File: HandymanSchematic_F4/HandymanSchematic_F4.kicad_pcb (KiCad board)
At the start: 4 copper layers, 55.6 x 45.5 mm, 79 parts, among them J1 SWD Header, J2 JACKS, J5 ScopeGroundLoop, Q1 BC847, Q2 2N7002, Q3 2N7002, SW1 RST, SW2 BYP, SW302 BOOT, U2 TL074, U3 STM32F411RETx, U4 AMS1117, U5 SSD1306, U6 TL072, Y1 16MHz

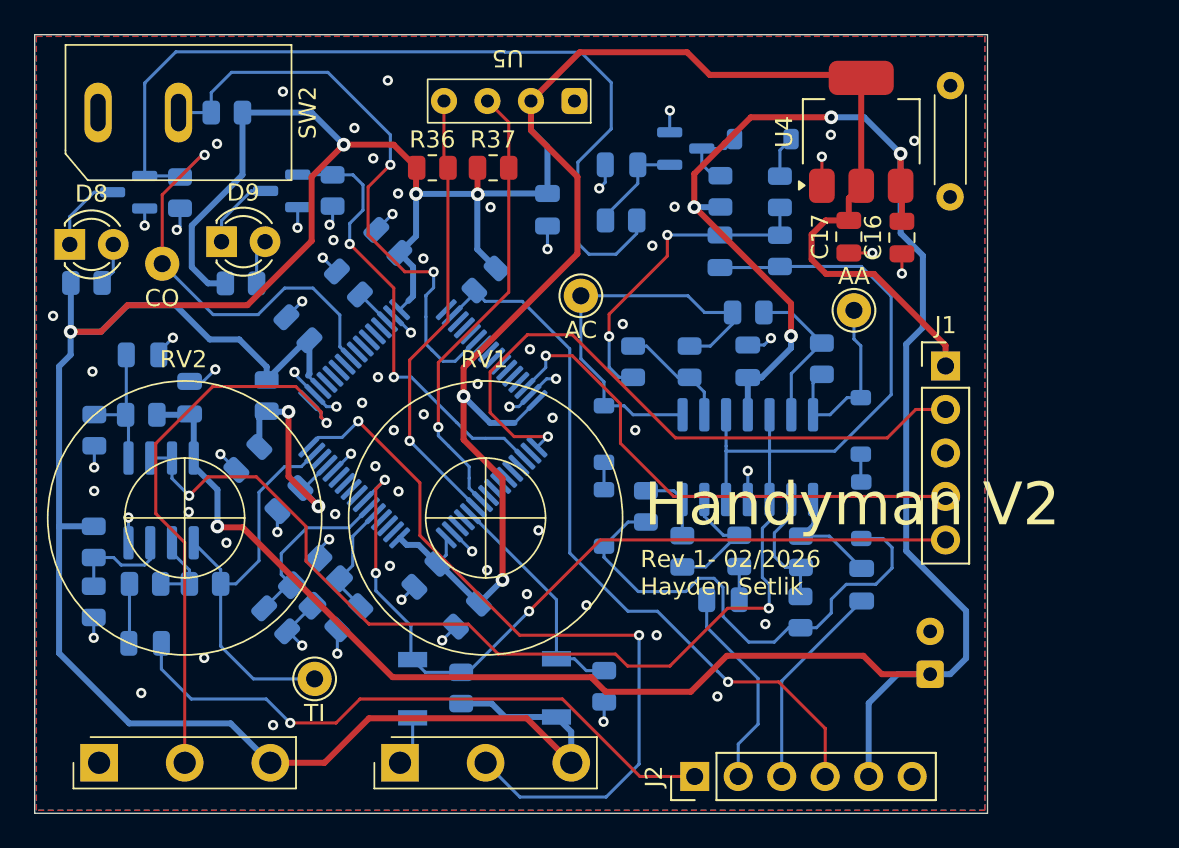
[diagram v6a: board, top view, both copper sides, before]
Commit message: slightly narrower board routed
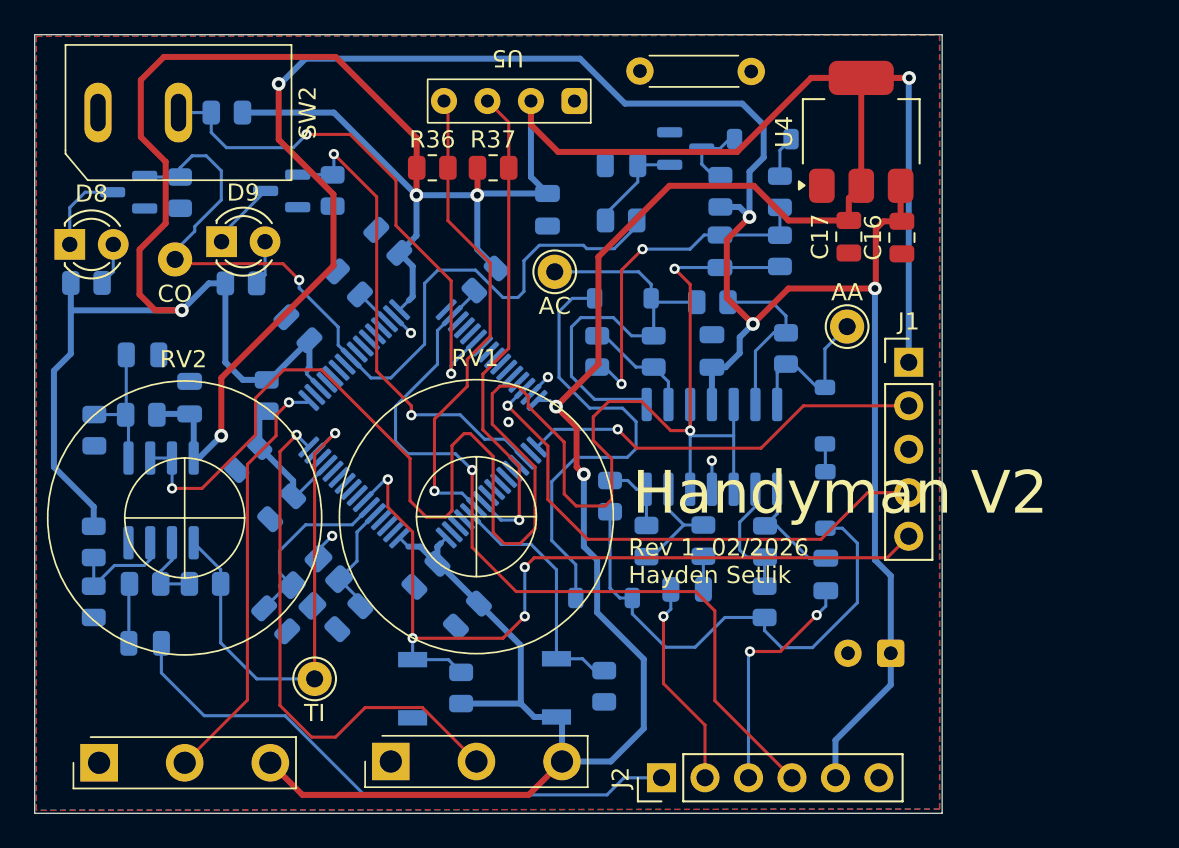
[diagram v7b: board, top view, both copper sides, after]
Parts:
- moved J5 15.5 mm to (38.4, 2.15), turned to 180 degrees
- moved D4 8.00 mm to (34.4, 15.4), turned to 180 degrees
- moved D5 4.68 mm to (33.3, 32.9), turned to 0 degrees
- moved C19 2.61 mm to (50.0, 36.1), turned to 180 degrees
- moved C6 2.18 mm to (38.1, 32.4)
- moved R10 2.18 mm to (32.9, 18.5)
- moved R12 2.18 mm to (35.7, 29.6)
- moved R15 2.18 mm to (33.6, 26.9)
- moved C10 2.18 mm to (46.2, 31.5)
- moved D7 2.18 mm to (46.2, 22.2)
- moved R13 2.18 mm to (36.2, 18.5)
- moved R18 2.18 mm to (39.6, 15.6)
- moved R19 2.18 mm to (42.6, 33.1)
- moved R21 2.18 mm to (43.9, 18.3)
- moved U2 2.18 mm to (39.6, 24.1)
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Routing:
- net GND: track 53.8 -> 6.18 mm, vias 76 -> 5
- net CLOSED_OUT: track 76.5 -> 51.3 mm
- net Net-(D4-A): track 1.60 -> 26.5 mm
- net /Analog/VG: track 89.5 -> 105.0 mm, vias 2 -> 3
- net SWCLK: track 37.9 -> 23.6 mm
- net THRESH_IN: track 45.0 -> 31.5 mm, vias 2 -> 1
- net RELEASE_IN: track 33.5 -> 24.8 mm
- net +9V: track 137.1 -> 128.7 mm
- net +3.3V: track 257.6 -> 265.7 mm
- net TUNE_IN: track 24.0 -> 29.4 mm, vias 0 -> 1
- net /Digital/TunerModeIn: track 42.9 -> 47.7 mm
- net +3.3VA: track 13.4 -> 8.68 mm, vias 2 -> 0
- net /Digital/GateByp: track 35.0 -> 30.9 mm
- net /Digital/SCL: track 26.7 -> 29.1 mm
- net FX_IN: track 36.4 -> 34.3 mm, vias 1 -> 0
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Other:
- board size 55.6 x 45.5 mm -> 53 x 45.5 mm

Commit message: routing prettified, stitching vias, silkscreen
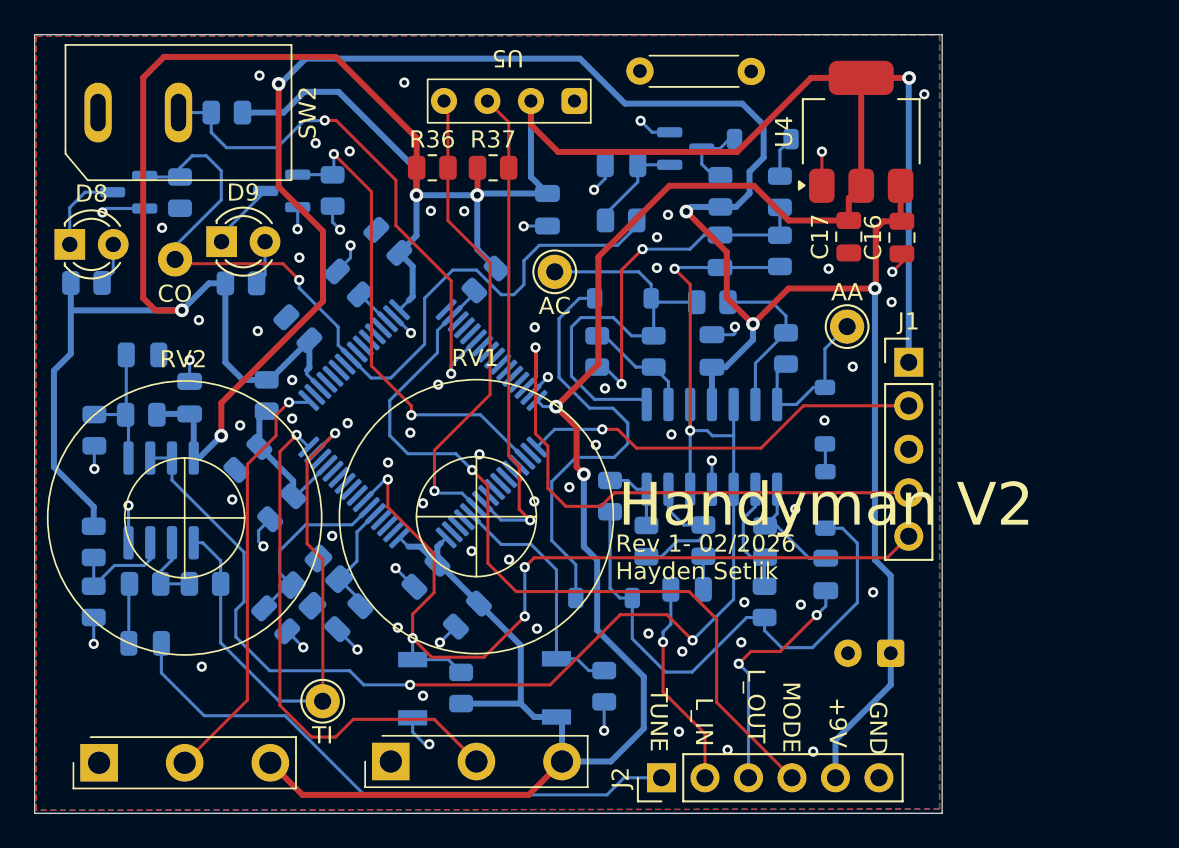
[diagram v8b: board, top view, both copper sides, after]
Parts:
- moved TP3 1.39 mm to (16.8, 38.9)
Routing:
- net GND: track 6.18 -> 40.8 mm, vias 5 -> 75
- net /Analog/VG: track 105.0 -> 82.2 mm, vias 3 -> 4
- net TUNE_IN: track 29.4 -> 32.6 mm
- net /Analog/SumPt: track 29.6 -> 31.6 mm
- net SWDIO: track 31.1 -> 33.1 mm
- net NRST: track 49.4 -> 51.3 mm
- net Net-(U2D--): track 6.55 -> 8.07 mm
- net Net-(D4-A): track 26.5 -> 25.1 mm
- net +9V: track 128.7 -> 129.8 mm
- net CLOSED_OUT: track 51.3 -> 50.3 mm
- net /Digital/GateByp: track 30.9 -> 31.6 mm
- net THRESH_IN: track 31.5 -> 30.9 mm
